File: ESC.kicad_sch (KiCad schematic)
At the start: 0 parts

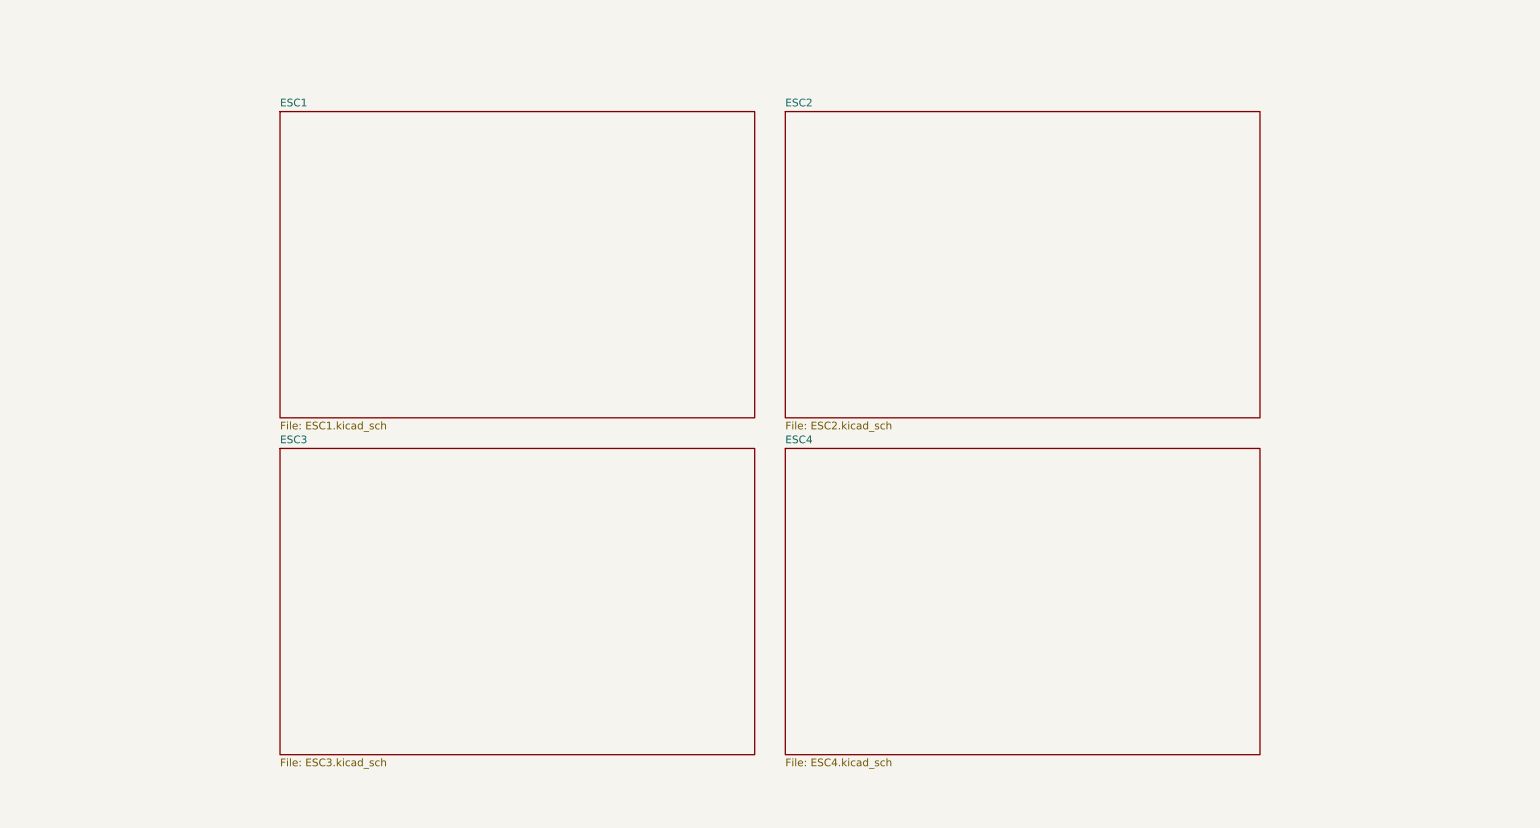
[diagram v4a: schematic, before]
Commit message: ESC design
Updated the ESC schematics.
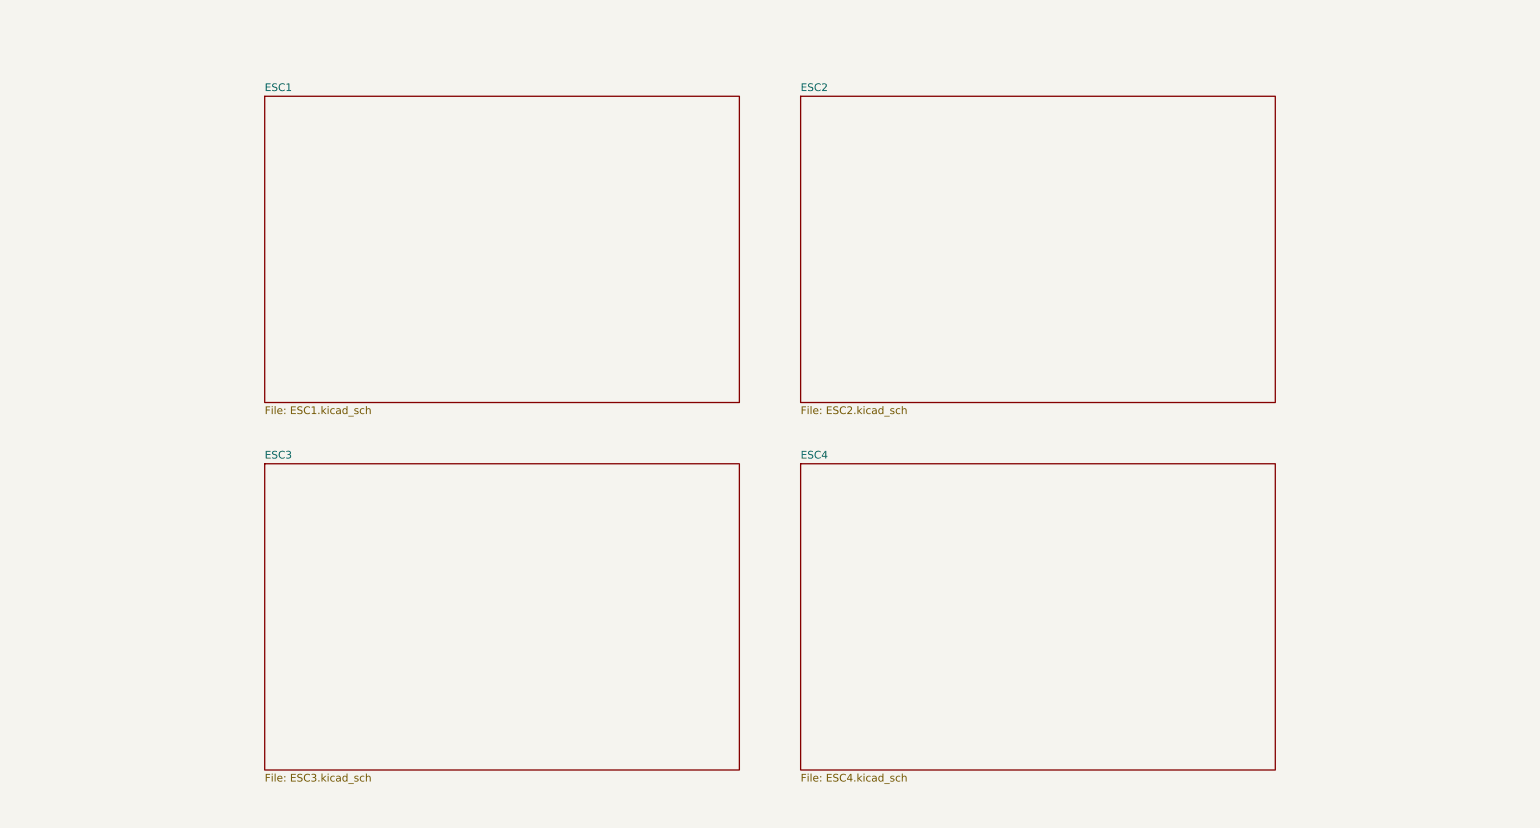
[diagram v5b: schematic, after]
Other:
- company: Chapuzas S.L. -> DavidMolTor
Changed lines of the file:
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@@
 		(date "2026-01-28")
 		(rev "1.0")
-		(company "Chapuzas S.L.")
+		(company "DavidMolTor")
 	)
 	(sheet
-		(at 66.04 38.1)
+		(at 63.5 35.56)
 		(size 78.74 50.8)
 		(exclude_from_sim no)
@@
 		)
 		(property "Sheetname" "ESC1"
-			(at 66.04 37.3884 0)
+			(at 63.5 34.8484 0)
 			(effects
 				(font
@@
 		)
 		(property "Sheetfile" "ESC1.kicad_sch"
-			(at 66.04 89.4846 0)
+			(at 63.5 86.9446 0)
 			(effects
 				(font
@@
 			(project "ThunderHorse"
 				(path "/ac187c6c-fa53-41cc-bce1-6f39a42a92e8/807a5f6f-4255-4cf0-8d90-acd62bb18590"
-					(page "7")
+					(page "5")
 				)
 			)
@@
 	)
 	(sheet
-		(at 149.86 38.1)
+		(at 152.4 35.56)
 		(size 78.74 50.8)
 		(exclude_from_sim no)
@@
 		)
 		(property "Sheetname" "ESC2"
-			(at 149.86 37.3884 0)
+			(at 152.4 34.8484 0)
 			(effects
 				(font
@@
 		)
 		(property "Sheetfile" "ESC2.kicad_sch"
-			(at 149.86 89.4846 0)
+			(at 152.4 86.9446 0)
+			(effects
+				(font
+					(size 1.27 1.27)
+				)
+				(justify left top)
+			)
+		)
+		(instances
+			(project "ThunderHorse"
+				(path "/ac187c6c-fa53-41cc-bce1-6f39a42a92e8/807a5f6f-4255-4cf0-8d90-acd62bb18590"
+					(page "6")
+				)
+			)
+		)
+	)
+	(sheet
+		(at 152.4 96.52)
+		(size 78.74 50.8)
+		(exclude_from_sim no)
+		(in_bom yes)
+		(on_board yes)
+		(dnp no)
+		(fields_autoplaced yes)
+		(stroke
+			(width 0.1524)
+			(type solid)
+		)
+		(fill
+			(color 0 0 0 0.0000)
+		)
+		(property "Sheetname" "ESC4"
+			(at 152.4 95.8084 0)
+			(effects
+				(font
+					(size 1.27 1.27)
+				)
+				(justify left bottom)
+			)
+		)
+		(property "Sheetfile" "ESC4.kicad_sch"
+			(at 152.4 147.9046 0)
 			(effects
 				(font
@@
 	)
 	(sheet
-		(at 149.86 93.98)
-		(size 78.74 50.8)
-		(exclude_from_sim no)
-		(in_bom yes)
-		(on_board yes)
-		(dnp no)
-		(fields_autoplaced yes)
-		(stroke
-			(width 0.1524)
-			(type solid)
-		)
-		(fill
-			(color 0 0 0 0.0000)
-		)
-		(property "Sheetname" "ESC4"
-			(at 149.86 93.2684 0)
-			(effects
-				(font
-					(size 1.27 1.27)
-				)
-				(justify left bottom)
-			)
-		)
-		(property "Sheetfile" "ESC4.kicad_sch"
-			(at 149.86 145.3646 0)
-			(effects
-				(font
-					(size 1.27 1.27)
-				)
-				(justify left top)
-			)
-		)
-		(instances
-			(project "ThunderHorse"
-				(path "/ac187c6c-fa53-41cc-bce1-6f39a42a92e8/807a5f6f-4255-4cf0-8d90-acd62bb18590"
-					(page "10")
-				)
-			)
-		)
-	)
-	(sheet
-		(at 66.04 93.98)
+		(at 63.5 96.52)
 		(size 78.74 50.8)
 		(exclude_from_sim no)
@@
 		)
 		(property "Sheetname" "ESC3"
-			(at 66.04 93.2684 0)
+			(at 63.5 95.8084 0)
 			(effects
 				(font
@@
 		)
 		(property "Sheetfile" "ESC3.kicad_sch"
-			(at 66.04 145.3646 0)
+			(at 63.5 147.9046 0)
 			(effects
 				(font
@@
 			(project "ThunderHorse"
 				(path "/ac187c6c-fa53-41cc-bce1-6f39a42a92e8/807a5f6f-4255-4cf0-8d90-acd62bb18590"
-					(page "9")
+					(page "7")
 				)
 			)
